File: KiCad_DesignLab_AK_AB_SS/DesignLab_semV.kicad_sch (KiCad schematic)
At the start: 31 parts, among them J1 Conn_01x04_Pin, J2 USB_C_Receptacle_USB2.0_16P, SW1 SW_Omron_B3FS, U1 ATmega328PB-A, U2 AMS1117-3.3, U3 CC56-12EWA, U4 DS18B20, U5 BMP280, U6 CH340N, Y1 Crystal

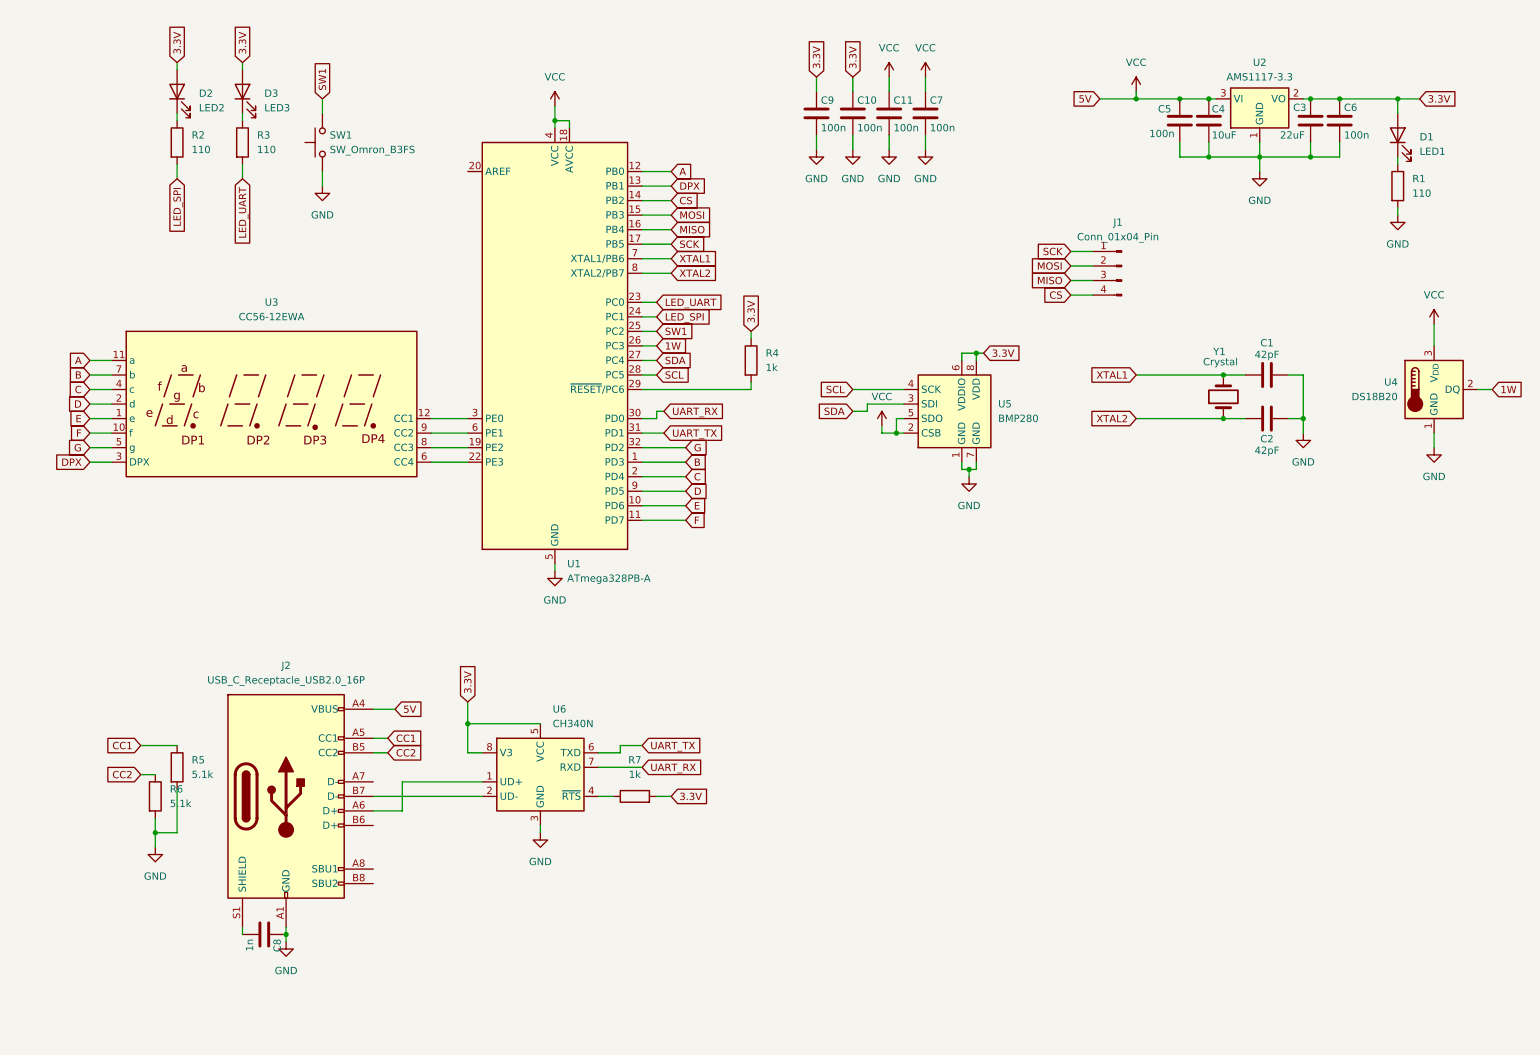
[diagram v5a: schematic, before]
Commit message: PCB layout modifications
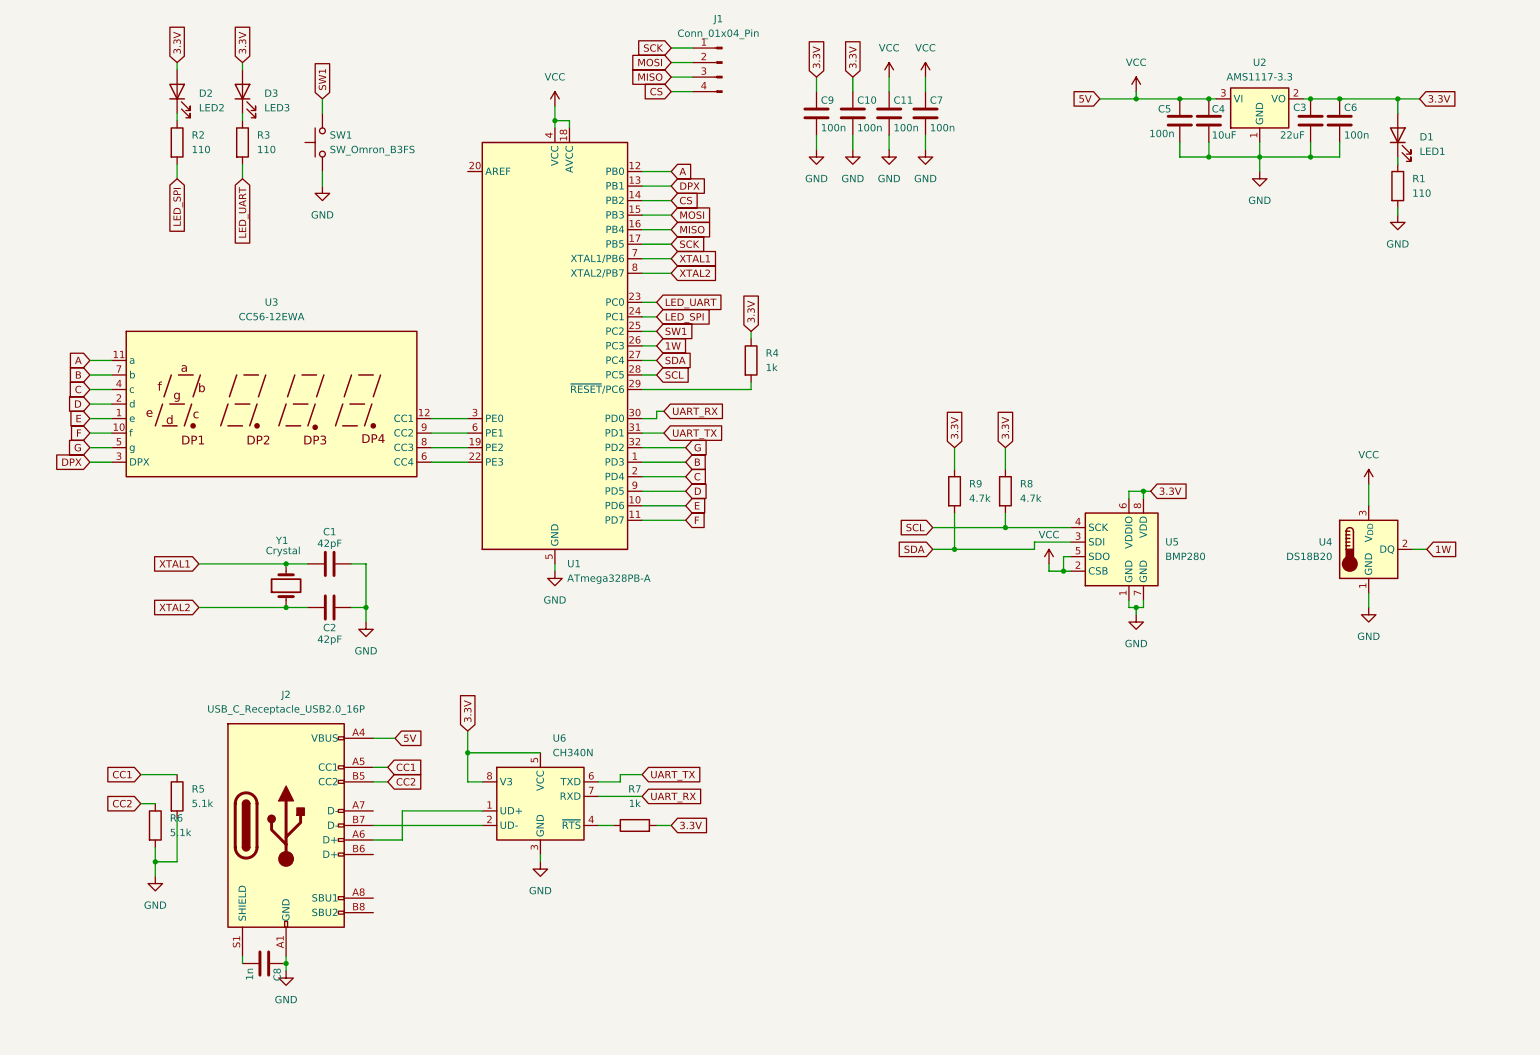
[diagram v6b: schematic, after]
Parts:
- added R8, R9: 4.7k, Resistor_SMD:R_0603_1608Metric, symbol Device:R
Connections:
- net 3.3V: now also R8.1, R9.1
- net SCL: now also R8.2
- net SDA: now also R9.2
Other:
- moved on the sheet: C1, C2, C8, J1, J2, R5, R6, R7, U4, U5, U6, Y1
